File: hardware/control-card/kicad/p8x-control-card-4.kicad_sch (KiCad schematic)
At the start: 2 parts, among them J1 MABC96R

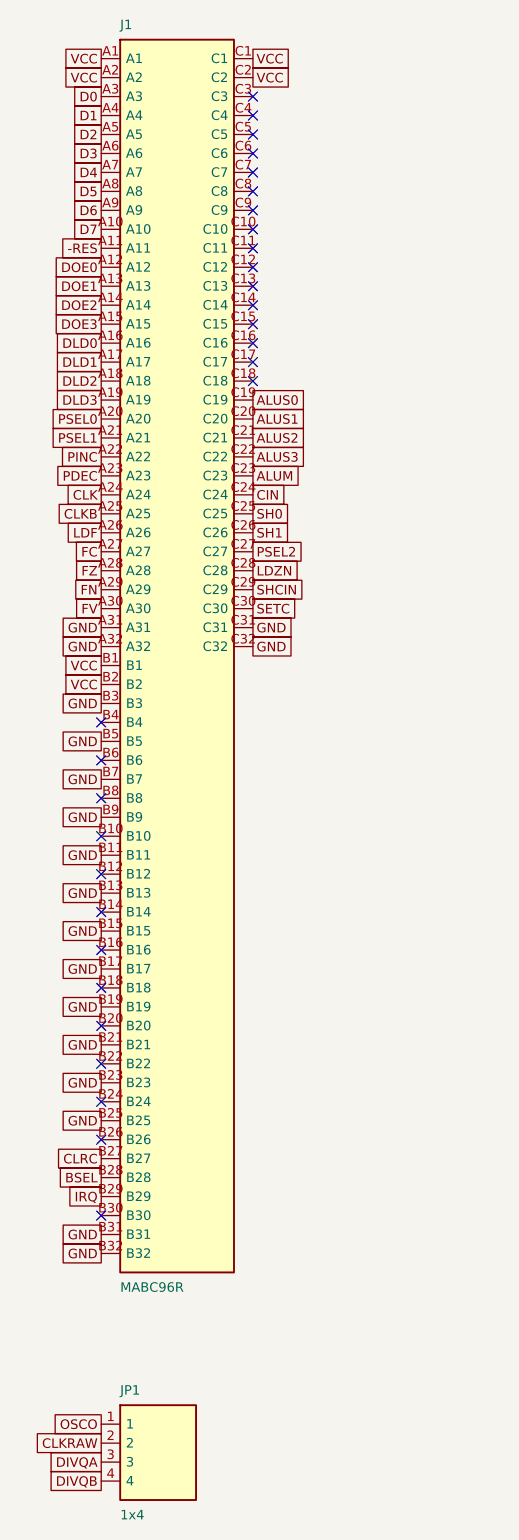
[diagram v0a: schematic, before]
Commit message: feat(sch): draw every P8X card schematic by function
Extend the functional-sheet grouping from the io-card to the control,
regbank, alu, memory, cf, ps2 and bustest cards. functional_sheets now
attaches unnamed glue gates, LEDs, resistors and connectors to the block
they share the most local nets with, so each block lists only its main
parts. A net with two or more pins on a sheet is now wired there even if
it continues elsewhere (its global name label rides on the wire), and
every wire is oriented by drawing side. The regbank gets one pointer per
sheet; the ps2 latches share a sheet with the AVR so the mailbox bus is
drawn. The bustest probe resistors use a straight-order RNISO8DSTR
drawing (the reversed B side forced every wire to cross and the sheet
fell back to labels). build_sch.sh now shows ELK fallbacks and clears old
numbered sheets before a build. All eight netlists match the boards,
ERC 0 errors; the boards change only in footprint link paths.

Co-Authored-By: Claude Opus 5.5 <noreply@anthropic.com>
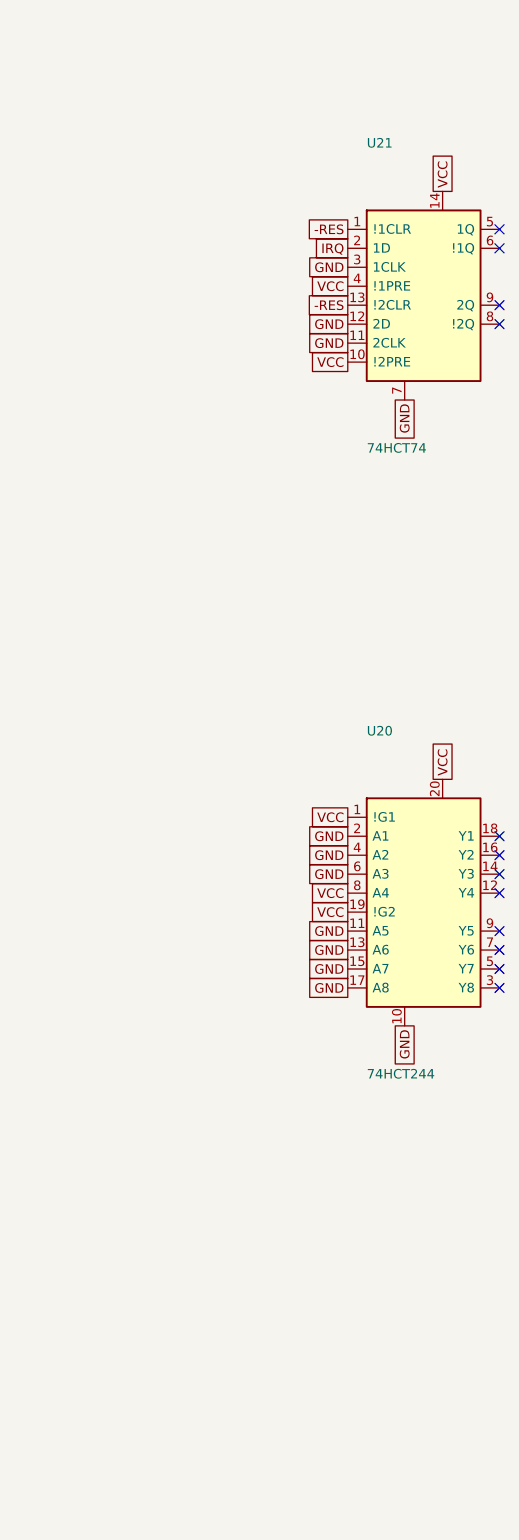
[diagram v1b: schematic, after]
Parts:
- removed J1: MABC96R, Connector_DIN:DIN41612_C_3x32_Male_Horizontal_THT, symbol p8x:DIN96C
- removed JP1: 1x4, Connector_PinHeader_2.54mm:PinHeader_1x04_P2.54mm_Vertical, symbol p8x:HDR4
- added U20: 74HCT244, Package_DIP:DIP-20_W7.62mm, symbol p8x:74244
- added U21: 74HCT74, Package_DIP:DIP-14_W7.62mm, symbol p8x:7474
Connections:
- net -RES: now also U21.1 (!1CLR), U21.13 (!2CLR)
- net GND: now also U20.10, U20.11 (A5), U20.13 (A6), U20.15 (A7), U20.17 (A8), U20.2 (A1), U20.4 (A2), U20.6 (A3), U21.11 (2CLK), U21.12 (2D), U21.3 (1CLK), U21.7
- net IRQ: now also U21.2 (1D)
- net VCC: now also U20.1 (!G1), U20.19 (!G2), U20.20, U20.8 (A4), U21.10 (!2PRE), U21.14, U21.4 (!1PRE)
- no-connect marks 29 -> 12
